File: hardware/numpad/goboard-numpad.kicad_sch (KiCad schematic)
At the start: 7 parts, among them J1 Conn_02x05_Top_Bottom, J2 Conn_01x01, J3 Conn_01x05, SW1 SW_Push

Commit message: Numpad: Connect the break-away-board to the main with traces
This allows software development without having to solder the LED to the
PCB with wires.
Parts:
- gave numbers to parts that had none: 1
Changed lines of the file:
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@@
   (symbol (lib_id "power:VCC") (at 41.91 119.38 0) (unit 1)
     (in_bom yes) (on_board yes)
-    (property "Reference" "#PWR?" (id 0) (at 41.91 123.19 0)
+    (property "Reference" "#PWR0115" (id 0) (at 41.91 123.19 0)
       (effects (font (size 1.27 1.27)) hide)
     )
@@
   (symbol (lib_id "Device:R") (at 41.91 125.73 0) (mirror y) (unit 1)
     (in_bom yes) (on_board yes)
-    (property "Reference" "R?" (id 0) (at 36.6838 125.73 90))
+    (property "Reference" "R2" (id 0) (at 36.6838 125.73 90))
     (property "Value" "10k" (id 1) (at 38.9825 125.73 90))
     (property "Footprint" "Resistor_SMD:R_0603_1608Metric_Pad0.98x0.95mm_HandSolder" (id 2) (at 43.688 125.73 90)
@@
     )
     (path "/3032a565-1b7e-4c02-98b0-0da7660dc986"
-      (reference "#PWR?") (unit 1) (value "VCC") (footprint "")
+      (reference "#PWR0115") (unit 1) (value "VCC") (footprint "")
     )
     (path "/07e3d3ae-4259-4c4b-b7e9-b71a69d216b3"
@@
       (reference "J3") (unit 1) (value "Conn_01x05") (footprint "Connector_PinHeader_2.54mm:PinHeader_1x05_P2.54mm_Vertical")
     )
+    (path "/11951edf-92e0-4cd6-abcd-c49336e8d01b"
+      (reference "R2") (unit 1) (value "10k") (footprint "Resistor_SMD:R_0603_1608Metric_Pad0.98x0.95mm_HandSolder")
+    )
     (path "/480f8756-d1de-4a1e-92bf-b0bdd56c4c78"
       (reference "R3") (unit 1) (value "1k") (footprint "Resistor_SMD:R_0603_1608Metric_Pad0.98x0.95mm_HandSolder")
     )
-    (path "/11951edf-92e0-4cd6-abcd-c49336e8d01b"
-      (reference "R?") (unit 1) (value "10k") (footprint "Resistor_SMD:R_0603_1608Metric_Pad0.98x0.95mm_HandSolder")
-    )
     (path "/9efc1083-5914-419f-bcd0-741b18f0726c"
       (reference "SW1") (unit 1) (value "SW_Push") (footprint "Button_Switch_SMD:SW_SPST_CK_RS282G05A3")
@@
     )
     (path "/abe4c75b-07ed-49c0-b60b-44793e4dbe28/29b831ea-d2be-48e7-b752-60c9497c4c1c"
-      (reference "#PWR?") (unit 1) (value "GND") (footprint "")
+      (reference "#PWR0116") (unit 1) (value "GND") (footprint "")
     )
     (path "/abe4c75b-07ed-49c0-b60b-44793e4dbe28/4e02c9aa-d56e-4c95-8573-62cac8b9c2d5"

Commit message: Numpad: Add power flag to satisfy the ERC
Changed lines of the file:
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@@
 (kicad_sch (version 20210126) (generator eeschema)
   (paper "A4")
+  (junction (at 32.385 34.29) (diameter 0.9144) (color 0 0 0 0))
   (junction (at 38.735 144.78) (diameter 0.9144) (color 0 0 0 0))
+  (junction (at 39.37 29.21) (diameter 0.9144) (color 0 0 0 0))
   (junction (at 41.91 131.445) (diameter 0.9144) (color 0 0 0 0))
   (no_connect (at 45.72 95.25))
   (no_connect (at 45.72 100.33))
   (no_connect (at 58.42 95.25))
-  (wire (pts (xy 29.21 34.29) (xy 34.29 34.29))
+  (wire (pts (xy 29.21 34.29) (xy 32.385 34.29))
     (stroke (width 0) (type solid) (color 0 0 0 0))
   )
@@
     (stroke (width 0) (type solid) (color 0 0 0 0))
   )
+  (wire (pts (xy 32.385 27.305) (xy 32.385 34.29))
+    (stroke (width 0) (type solid) (color 0 0 0 0))
+  )
+  (wire (pts (xy 32.385 34.29) (xy 34.29 34.29))
+    (stroke (width 0) (type solid) (color 0 0 0 0))
+  )
   (wire (pts (xy 32.385 144.78) (xy 38.735 144.78))
     (stroke (width 0) (type solid) (color 0 0 0 0))
@@
   )
   (wire (pts (xy 39.37 29.21) (xy 39.37 31.75))
+    (stroke (width 0) (type solid) (color 0 0 0 0))
+  )
+  (wire (pts (xy 39.37 29.21) (xy 47.625 29.21))
     (stroke (width 0) (type solid) (color 0 0 0 0))
   )
@@
   (label "SWDCLK" (at 86.36 96.52 0)
     (effects (font (size 1.27 1.27)) (justify left bottom))
+  )
+  (symbol (lib_id "power:PWR_FLAG") (at 32.385 27.305 0) (unit 1)
+    (in_bom yes) (on_board yes)
+    (property "Reference" "#FLG0102" (id 0) (at 32.385 25.4 0)
+      (effects (font (size 1.27 1.27)) hide)
+    )
+    (property "Value" "PWR_FLAG" (id 1) (at 32.385 22.9806 0))
+    (property "Footprint" "" (id 2) (at 32.385 27.305 0)
+      (effects (font (size 1.27 1.27)) hide)
+    )
+    (property "Datasheet" "~" (id 3) (at 32.385 27.305 0)
+      (effects (font (size 1.27 1.27)) hide)
+    )
+    (pin "1")
+  )
+  (symbol (lib_id "power:PWR_FLAG") (at 47.625 29.21 180) (unit 1)
+    (in_bom yes) (on_board yes)
+    (property "Reference" "#FLG0101" (id 0) (at 47.625 31.115 0)
+      (effects (font (size 1.27 1.27)) hide)
+    )
+    (property "Value" "PWR_FLAG" (id 1) (at 47.625 33.5344 0))
+    (property "Footprint" "" (id 2) (at 47.625 29.21 0)
+      (effects (font (size 1.27 1.27)) hide)
+    )
+    (property "Datasheet" "~" (id 3) (at 47.625 29.21 0)
+      (effects (font (size 1.27 1.27)) hide)
+    )
+    (pin "1")
   )
   (symbol (lib_id "power:VCC") (at 34.29 33.02 0) (unit 1)
@@
   )
   (symbol_instances
+    (path "/e6fe5c92-e732-45bc-b06a-c3a3df805e1d"
+      (reference "#FLG0101") (unit 1) (value "PWR_FLAG") (footprint "")
+    )
+    (path "/500376f8-5258-4ab6-aafe-d4658edec5fb"
+      (reference "#FLG0102") (unit 1) (value "PWR_FLAG") (footprint "")
+    )
     (path "/44074299-6d39-4fba-9012-33f74a761aad"
       (reference "#PWR0101") (unit 1) (value "VCC") (footprint "")

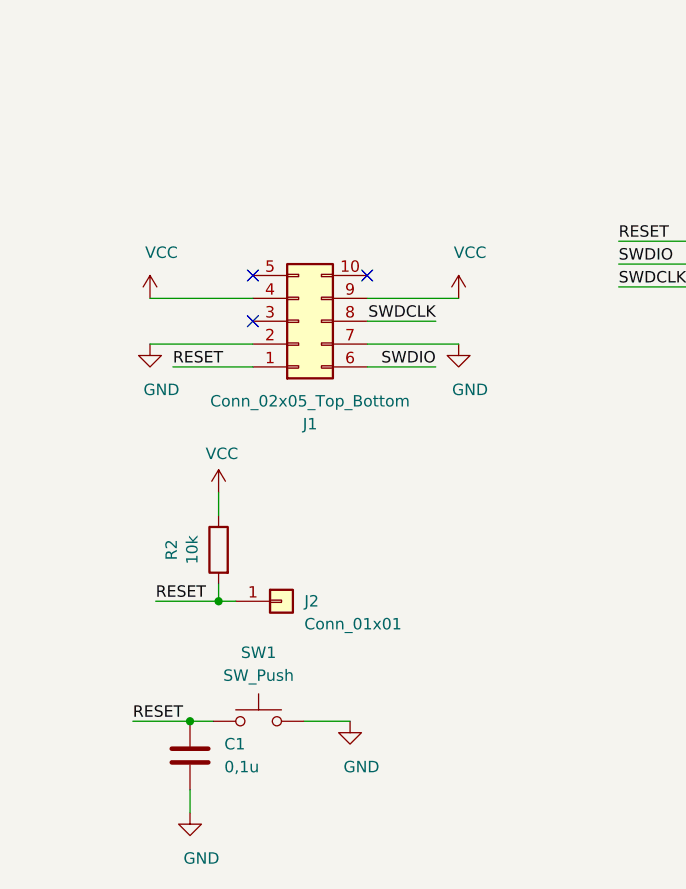
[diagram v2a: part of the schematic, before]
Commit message: Main & Numpad: Fix the pin-out of the programmer connector
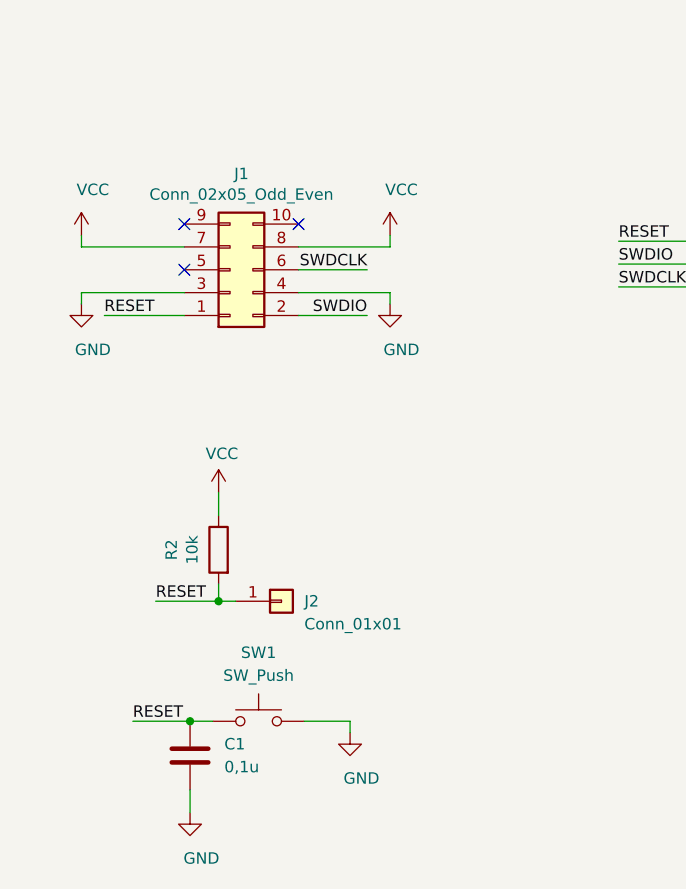
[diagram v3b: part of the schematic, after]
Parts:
- removed J1: Conn_02x05_Top_Bottom, footprints:programming_port_st_link_clone_without_silkscreen_outline, symbol Connector_Generic:Conn_02x05_Top_Bottom
- added J1: Conn_02x05_Odd_Even, footprints:programming_port_st_link_clone_without_silkscreen_outline, symbol Connector_Generic:Conn_02x05_Odd_Even
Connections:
- net GND: now also J1.3 (Pin_3), J1.4 (Pin_4)
- net RESET: now also J1.1 (Pin_1)
- net SWDCLK: now also J1.6 (Pin_6)
- net SWDIO: now also J1.2 (Pin_2)
- net VCC: now also J1.7 (Pin_7), J1.8 (Pin_8)

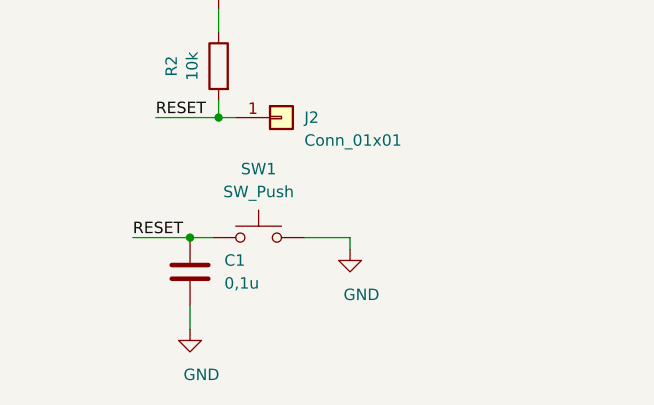
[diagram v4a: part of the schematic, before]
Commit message: Main & Numpad: Exchange unavailable capacitors
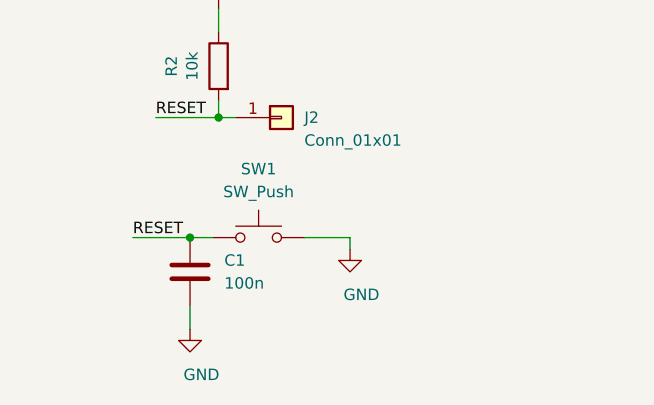
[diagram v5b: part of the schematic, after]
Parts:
- C1: value 0,1u -> 100n; Mouser 581-0603YC104MAT4A -> 581-0603YC104MAT4A
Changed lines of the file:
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@@
       (effects (font (size 1.27 1.27)) (justify left))
     )
-    (property "Value" "0,1u" (id 1) (at 42.545 149.86 0)
+    (property "Value" "100n" (id 1) (at 42.545 149.86 0)
       (effects (font (size 1.27 1.27)) (justify left))
     )
@@
       (effects (font (size 1.27 1.27)) hide)
     )
-    (property "Mouser" "581-0603YC104MAT4A" (id 4) (at 38.735 148.59 0)
+    (property "Mouser" "581-0603YC104MAT4A " (id 4) (at 38.735 148.59 0)
       (effects (font (size 1.27 1.27)) hide)
     )
@@
     )
     (path "/07e3d3ae-4259-4c4b-b7e9-b71a69d216b3"
-      (reference "C1") (unit 1) (value "0,1u") (footprint "Capacitor_SMD:C_0603_1608Metric_Pad1.08x0.95mm_HandSolder")
+      (reference "C1") (unit 1) (value "100n") (footprint "Capacitor_SMD:C_0603_1608Metric_Pad1.08x0.95mm_HandSolder")
     )
     (path "/2f5f2715-b384-4980-89ad-44e7d3193b72"

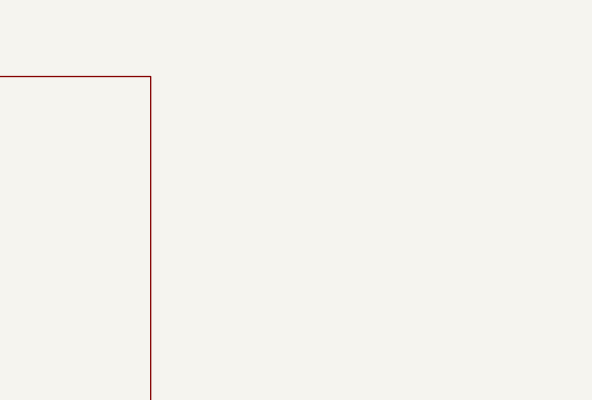
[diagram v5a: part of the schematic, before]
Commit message: Numpad: Add mounting holes
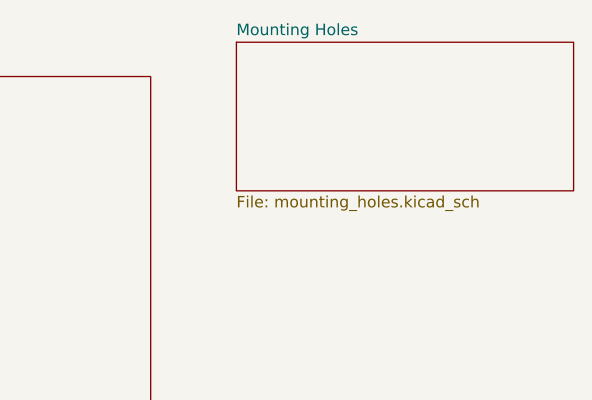
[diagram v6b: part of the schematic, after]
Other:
- added sheet Mounting Holes (mounting_holes.kicad_sch)
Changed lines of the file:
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@@
+    )
+  )
+  (sheet (at 243.205 21.59) (size 37.465 16.51)
+    (stroke (width 0.001) (type solid) (color 132 0 132 1))
+    (fill (color 255 255 255 0.0000))
+    (property "Sheet name" "Mounting Holes" (id 0) (at 243.205 20.9541 0)
+      (effects (font (size 1.27 1.27)) (justify left bottom))
+    )
+    (property "Sheet file" "mounting_holes.kicad_sch" (id 1) (at 243.205 38.6089 0)
+      (effects (font (size 1.27 1.27)) (justify left top))
     )
   )
@@
     (path "/7cad715e-ebc0-41a5-9955-927ca63abd2f/" (page "2"))
     (path "/abe4c75b-07ed-49c0-b60b-44793e4dbe28/" (page "3"))
+    (path "/4c67ad73-5e6f-4035-9a7f-f7592c55e47c/" (page "4"))
   )
   (symbol_instances
@@
       (reference "U1") (unit 1) (value "STM32L031F6Px") (footprint "Package_SO:TSSOP-20_4.4x6.5mm_P0.65mm")
     )
-  )
+    (path "/4c67ad73-5e6f-4035-9a7f-f7592c55e47c/686ad52d-175f-4948-a446-6098284ce702"
+      (reference "H1") (unit 1) (value "MountingHole") (footprint "MountingHole:MountingHole_2.2mm_M2_Pad")
+    )
+    (path "/4c67ad73-5e6f-4035-9a7f-f7592c55e47c/0949fb46-5fea-405a-b192-1cadccaec76f"
+      (reference "H2") (unit 1) (value "MountingHole") (footprint "MountingHole:MountingHole_2.2mm_M2_Pad")
+    )
+    (path "/4c67ad73-5e6f-4035-9a7f-f7592c55e47c/51147556-2c4b-47aa-a309-d9d5d9edecb1"
+      (reference "H3") (unit 1) (value "MountingHole") (footprint "MountingHole:MountingHole_2.2mm_M2_Pad")
+    )
+    (path "/4c67ad73-5e6f-4035-9a7f-f7592c55e47c/2fd2ca89-2f68-480e-820c-86f6d116d475"
+      (reference "H4") (unit 1) (value "MountingHole") (footprint "MountingHole:MountingHole_2.2mm_M2_Pad")
+    )
+    (path "/4c67ad73-5e6f-4035-9a7f-f7592c55e47c/5697db13-10da-4041-8a98-5ca70b1ac21b"
+      (reference "H5") (unit 1) (value "MountingHole") (footprint "MountingHole:MountingHole_2.2mm_M2_Pad")
+    )
+  )
